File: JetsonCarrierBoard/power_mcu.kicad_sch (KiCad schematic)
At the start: 7 parts

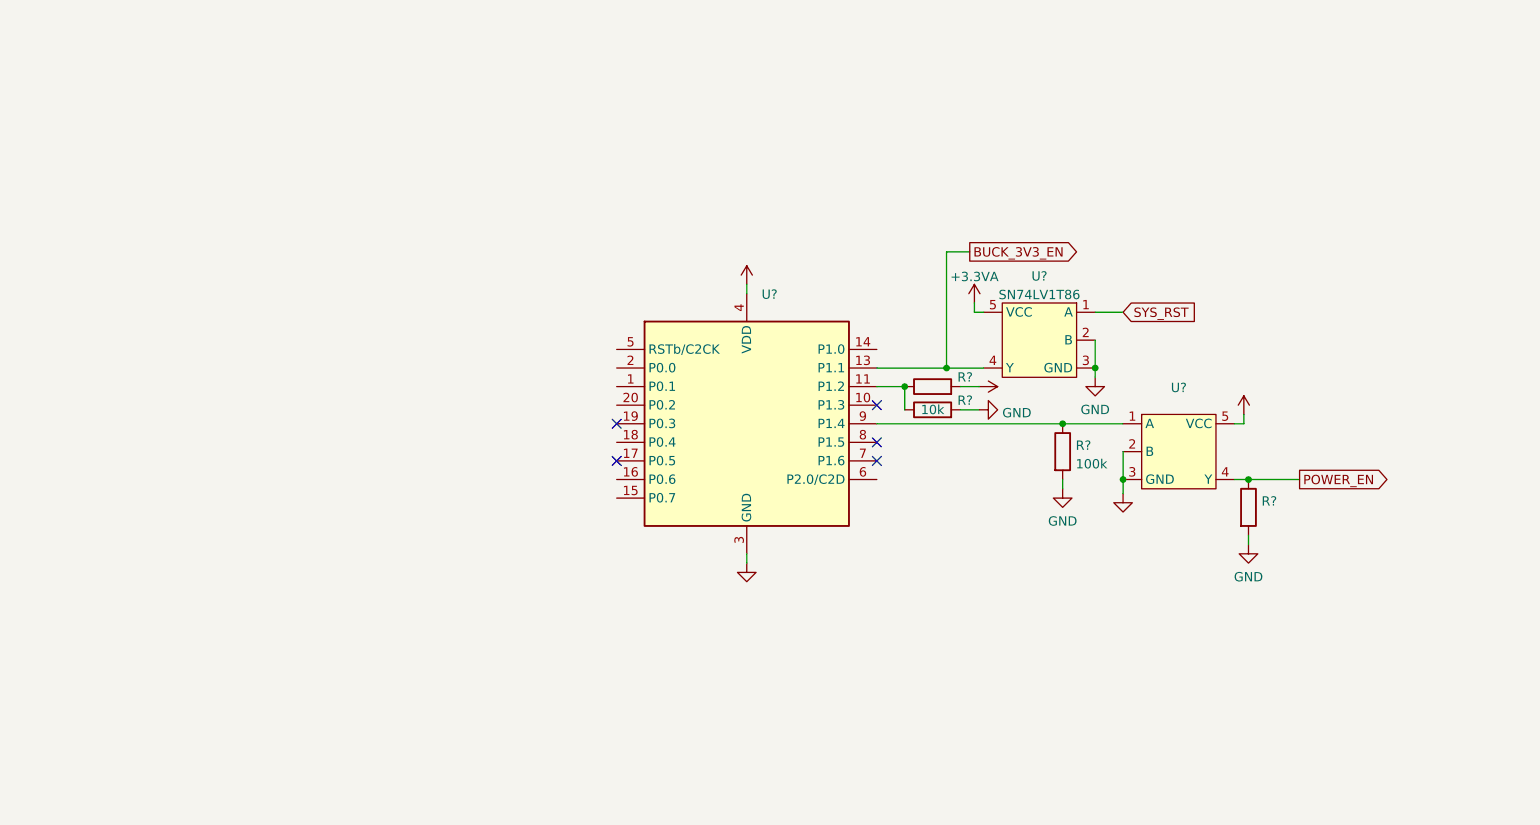
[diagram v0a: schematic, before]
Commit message: Fan and Debug UART
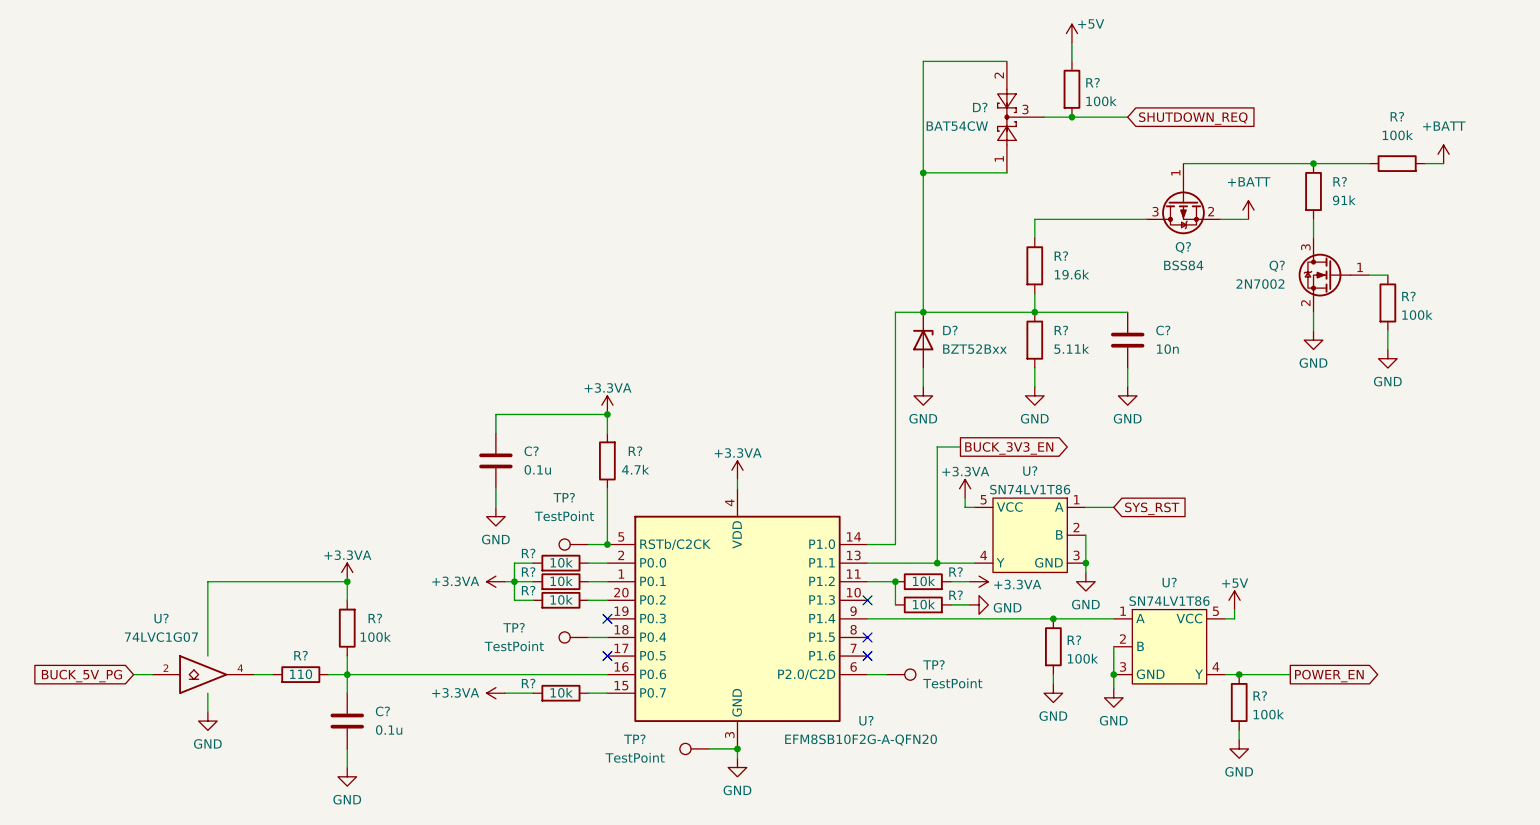
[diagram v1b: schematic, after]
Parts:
- added C? (x2): 0.1u, symbol Device:C
- added C?: 10n, symbol Device:C
- added D?: BAT54CW, Package_TO_SOT_SMD:SOT-323_SC-70, symbol Diode:BAT54CW
- added D?: BZT52Bxx, Diode_SMD:D_SOD-123F, symbol Diode:BZT52Bxx
- added Q?: BSS84, Package_TO_SOT_SMD:SOT-23, symbol Transistor_FET:BSS84
- added Q?: 2N7002, Package_TO_SOT_SMD:SOT-23, symbol Transistor_FET:2N7002
- added R?: 4.7k, symbol Device:R
- added R?: 5.11k, symbol Device:R
- added R?: 91k, symbol Device:R
- added R? (x4): 100k, symbol Device:R
- added R? (x4): 10k, symbol Device:R
- added R?: 110, symbol Device:R
- added R?: 19.6k, symbol Device:R
- added TP? (x4): TestPoint, symbol Connector:TestPoint
- added U?: 74LVC1G07, symbol 74xGxx:74LVC1G07
- R?: value (none) -> 100k
- R?: value (none) -> 10k
- U?: value (none) -> SN74LV1T86
- U?: value (none) -> EFM8SB10F2G-A-QFN20; footprint (none) -> Package_DFN_QFN:SiliconLabs_QFN-20-1EP_3x3mm_P0.5mm_EP1.8x1.8mm
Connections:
- net +3.3VA: now also C?.1, R?.2, R?.2, R?.2, R?.2, R?.2, R?.2, U?.5 (VCC)
- net +5V: now also R?.1
- net GND: now also C?.2, C?.2, C?.2, D?.2 (A), Q?.2 (S), R?.2, R?.2, TP?.1, U?.3 (GND)
- net at U?.1 (P0.1): now also R?.1
- net at U?.14 (P1.0): now also C?.1, D?.1, D?.1 (K), D?.2, R?.1, R?.2
- net at U?.15 (P0.7): now also R?.1
- net at U?.16 (P0.6): now also C?.1, R?.1, R?.1
- net at U?.18 (P0.4): now also TP?.1
- net at U?.2 (P0.0): now also R?.1
- net at U?.20 (P0.2): now also R?.1
- net at U?.5 (RSTb/C2CK): now also R?.1, TP?.1
- net at U?.6 (P2.0/C2D): now also TP?.1
- new net: Q?.1 (G), R?.1, R?.1
- new net: Q?.3 (D), R?.1
- new net: Q?.3 (D), R?.2
- new net: Q?.1 (G), R?.1
- new net: R?.2, U?.4
- new net +BATT: Q?.2 (S), R?.2
- new net BUCK_5V_PG: U?.2
- new net SHUTDOWN_REQ: D?.3, R?.2
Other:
- moved on the sheet: R?, U?

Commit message: Connections
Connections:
- net SYS_RST renamed SYS_RST*
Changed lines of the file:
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@@
     )
   )
-  (global_label "SYS_RST" (shape input) (at 200.025 106.68 0) (fields_autoplaced)
+  (global_label "SYS_RST*" (shape input) (at 200.025 106.68 0) (fields_autoplaced)
     (effects (font (size 1.27 1.27)) (justify left))
-    (property "Intersheet References" "${INTERSHEET_REFS}" (id 0) (at 210.3605 106.6006 0)
+    (property "Intersheet References" "${INTERSHEET_REFS}" (id 0) (at 211.3281 106.6006 0)
       (effects (font (size 1.27 1.27)) (justify left) hide)
     )

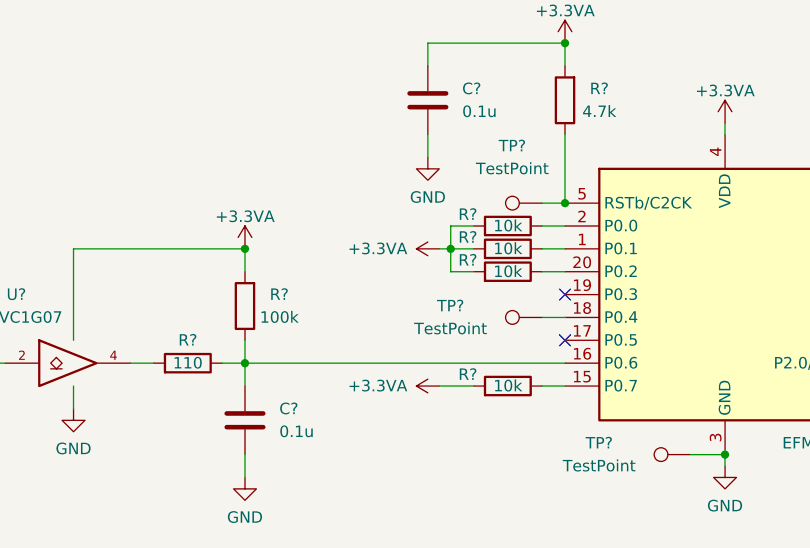
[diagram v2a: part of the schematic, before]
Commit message: Button Header Pinout wiring
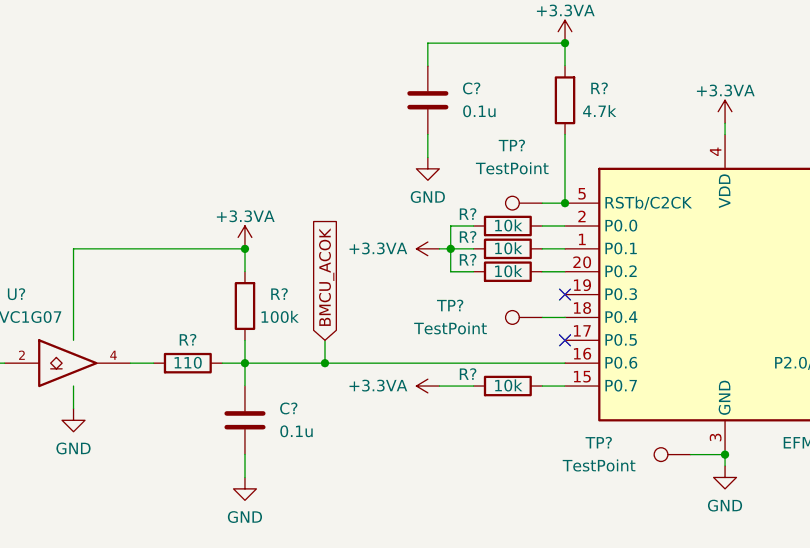
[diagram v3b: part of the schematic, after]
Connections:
- net BMCU_ACOK: now reaches C?.1, R?.1, R?.1, U?.16 (P0.6)
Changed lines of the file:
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@@
   (junction (at 196.215 114.3) (diameter 0) (color 0 0 0 0)
+  )
+  (junction (at 104.14 129.54) (diameter 0) (color 0 0 0 0)
   )
   (junction (at 191.77 121.92) (diameter 0) (color 0 0 0 0)
@@
     (stroke (width 0) (type default) (color 0 0 0 0))
   )
+  (wire (pts (xy 104.14 129.54) (xy 130.81 129.54))
+    (stroke (width 0) (type default) (color 0 0 0 0))
+  )
   (wire (pts (xy 190.5 53.34) (xy 194.31 53.34))
     (stroke (width 0) (type default) (color 0 0 0 0))
@@
     (stroke (width 0) (type default) (color 0 0 0 0))
   )
+  (wire (pts (xy 104.14 127) (xy 104.14 129.54))
+    (stroke (width 0) (type default) (color 0 0 0 0))
+  )
   (wire (pts (xy 170.18 80.01) (xy 173.99 80.01))
     (stroke (width 0) (type default) (color 0 0 0 0))
@@
     (stroke (width 0) (type default) (color 0 0 0 0))
   )
-  (wire (pts (xy 95.25 129.54) (xy 130.81 129.54))
+  (wire (pts (xy 95.25 129.54) (xy 104.14 129.54))
     (stroke (width 0) (type default) (color 0 0 0 0))
   )
@@
       (effects (font (size 1.27 1.27)) (justify left) hide)
     )
+  )
+  (global_label "BMCU_ACOK" (shape input) (at 104.14 127 90) (fields_autoplaced)
+    (effects (font (size 1.27 1.27)) (justify left))
+    (property "Intersheet References" "${INTERSHEET_REFS}" (id 0) (at 104.0606 113.3383 90)
+      (effects (font (size 1.27 1.27)) (justify left) hide)
+    )

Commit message: Adding more Title block info and changing main hierarchical page layout
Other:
- title: (none) -> Power Management MCU
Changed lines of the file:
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@@
 (kicad_sch (version 20211123) (generator eeschema)
   (paper "A4")
+  (title_block
+    (title "Power Management MCU")
+    (date "2022-09-18")
+    (rev "1.0")
+  )
   (junction (at 200.025 129.54) (diameter 0) (color 0 0 0 0)
   )

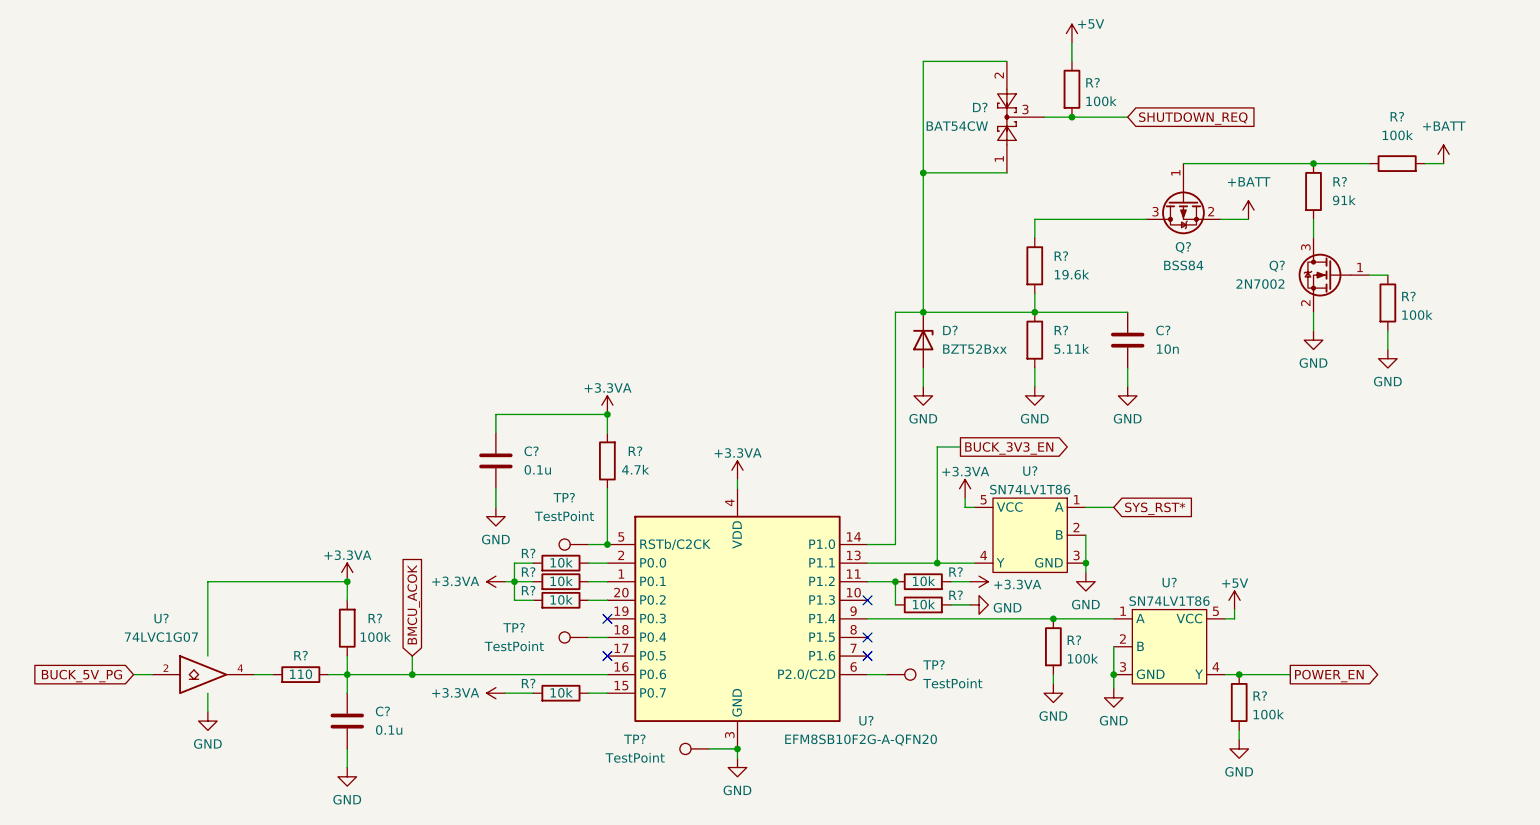
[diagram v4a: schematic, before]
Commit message: Improvement list, fixes, and readability improvements
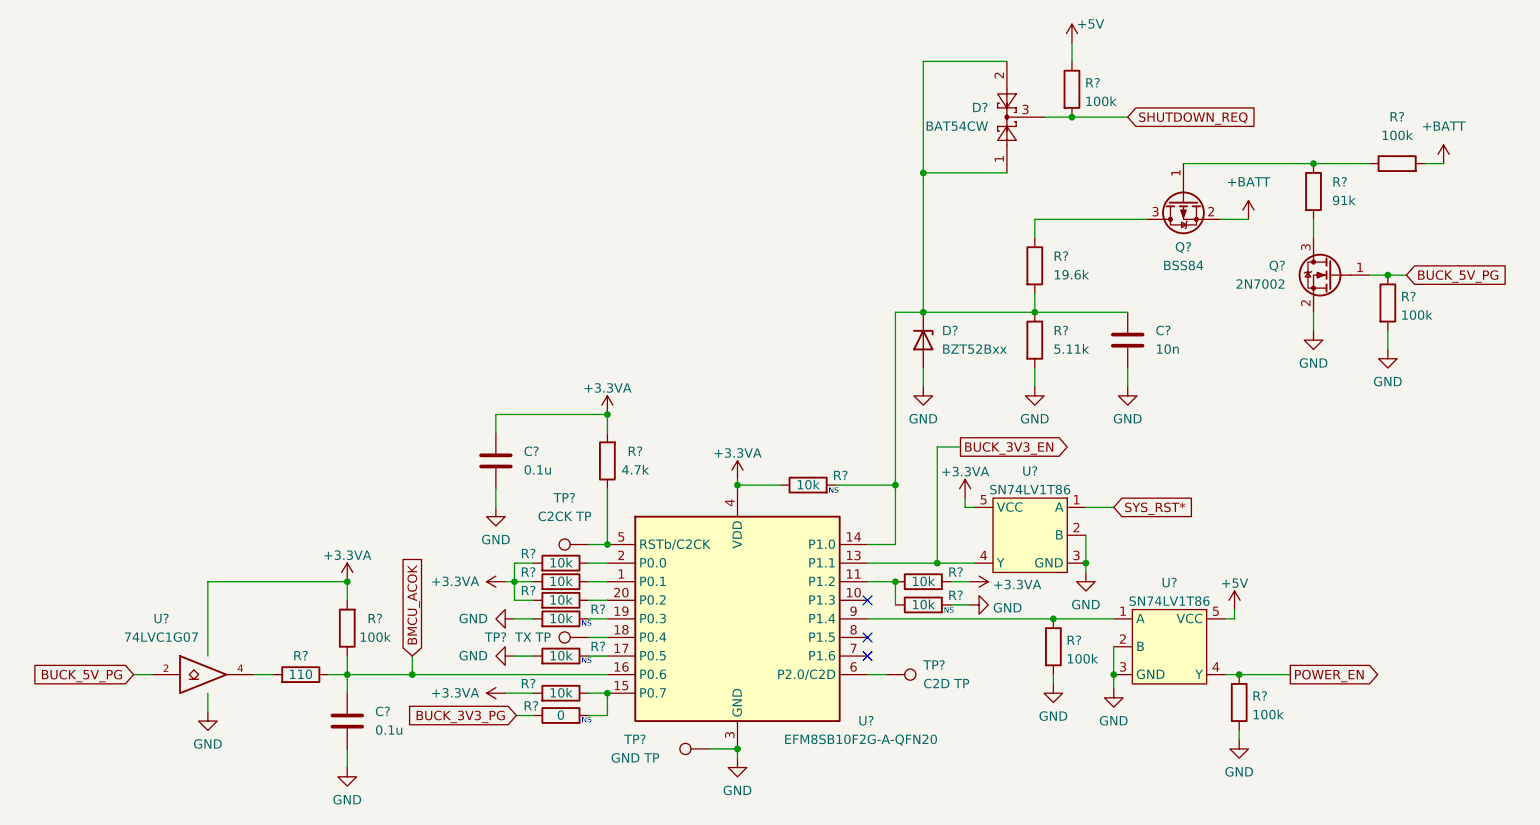
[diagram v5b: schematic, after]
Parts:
- added R? (x3): 10k, symbol Device:R
- added R?: 0, symbol Device:R
- TP?: value TestPoint -> TX TP
- TP?: value TestPoint -> C2D TP
- TP?: value TestPoint -> GND TP
- TP?: value TestPoint -> C2CK TP
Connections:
- net +3.3VA: now also R?.1
- net BUCK_5V_PG: now also Q?.1 (G), R?.1
- net GND: now also R?.2, R?.2
- net at C?.1, D?.1, D?.1 (K)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: now also R?.2
- net at R?.1, U?.15 (P0.7): now also R?.2
- net at U?.17 (P0.5): now also R?.1
- net at U?.19 (P0.3): now also R?.1
- new net BUCK_3V3_PG: R?.1
- no-connect marks 5 -> 3
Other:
- note added: "NS"
